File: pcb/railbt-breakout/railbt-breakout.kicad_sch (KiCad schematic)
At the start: 6 parts, among them J1 RJ45, J2 RJ45, J3 Conn_01x04_Pin, Q1 BC108, U1 XL1509-5.0

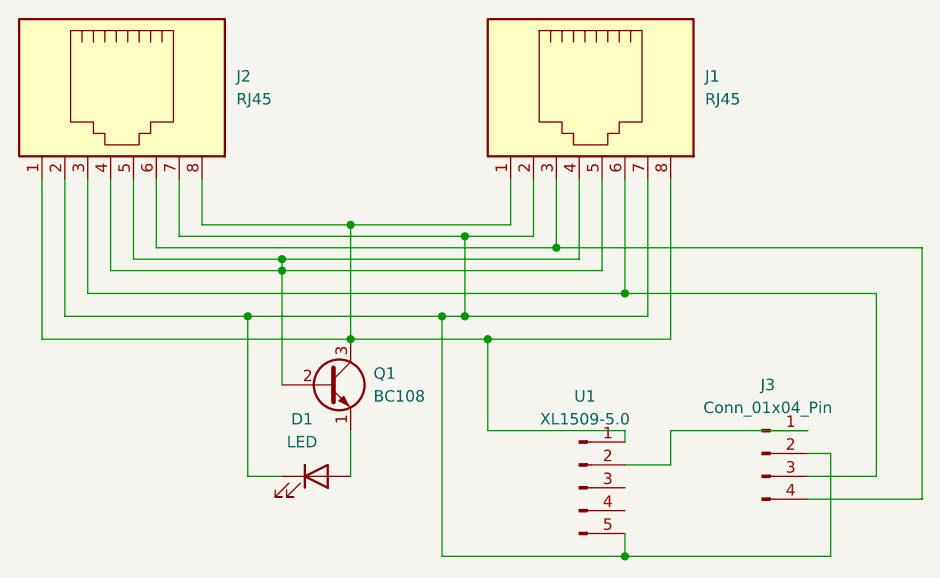
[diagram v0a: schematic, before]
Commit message: Update PCB to latest revision
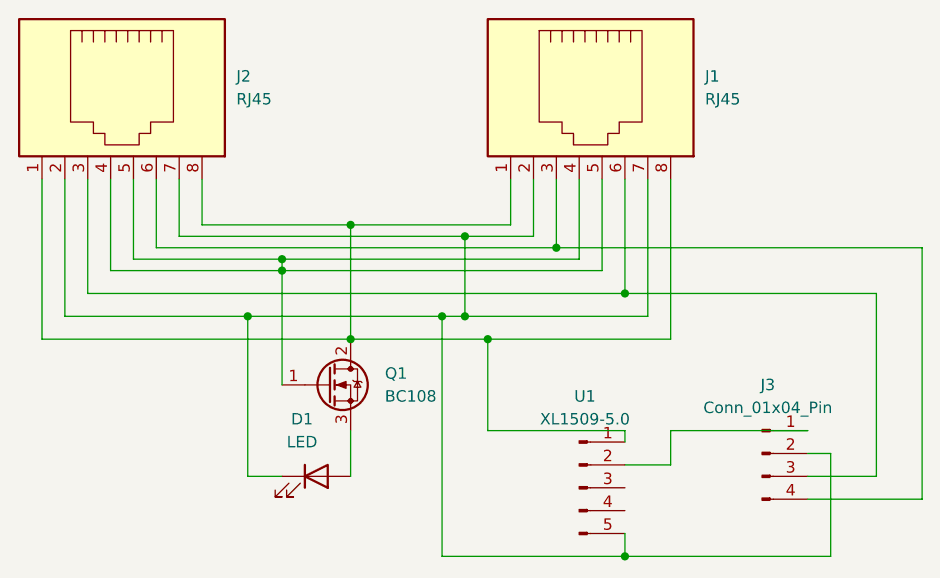
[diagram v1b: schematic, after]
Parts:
- Q1: footprint Package_TO_SOT_THT:TO-18-3 -> Package_TO_SOT_THT:TO-220-3_Vertical; symbol Transistor_BJT:BC108 -> Transistor_FET:IRLZ34N
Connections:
- net at J1.1, J1.8, J2.1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: now also Q1.2 (D); no longer Q1.3 (C)
- net at J1.4, J1.5, J2.4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: now also Q1.1 (G); no longer Q1.2 (B)
- net at D1.2 (A): now also Q1.3 (S); no longer Q1.1 (E)
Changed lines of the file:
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@@
 	)
 	(symbol
-		(lib_id "Transistor_BJT:BC108")
+		(lib_id "Transistor_FET:IRLZ34N")
 		(at 156.21 67.31 0)
 		(unit 1)
@@
 		(fields_autoplaced yes)
 		(property "Reference" "Q1"
-			(at 161.29 66.0399 0)
+			(at 162.56 66.0399 0)
 			(effects
 				(font
@@
 		)
 		(property "Value" "BC108"
-			(at 161.29 68.5799 0)
+			(at 162.56 68.5799 0)
 			(effects
 				(font
@@
 			)
 		)
-		(property "Footprint" "Package_TO_SOT_THT:TO-18-3"
+		(property "Footprint" "Package_TO_SOT_THT:TO-220-3_Vertical"
 			(at 161.29 69.215 0)
 			(effects
@@
 			)
 		)
-		(property "Datasheet" "http://www.b-kainka.de/Daten/Transistor/BC108.pdf"
-			(at 156.21 67.31 0)
+		(property "Datasheet" "http://www.infineon.com/dgdl/irlz34npbf.pdf?fileId=5546d462533600a40153567206892720"
+			(at 161.29 71.12 0)
 			(effects
 				(font
@@
 			)
 		)
-		(property "Description" "0.1A Ic, 30V Vce, Low Noise General Purpose NPN Transistor, TO-18"
+		(property "Description" "30A Id, 55V Vds, 35mOhm Rds, N-Channel HEXFET Power MOSFET, TO-220AB"
 			(at 156.21 67.31 0)
 			(effects
